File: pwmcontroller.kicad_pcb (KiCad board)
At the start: 2 copper layers, 35.1 x 44.5 mm, 19 parts, among them J1 CONN_01X04, J2 CONN_01X04, U1 WPMIx9200501S, U2 NE555

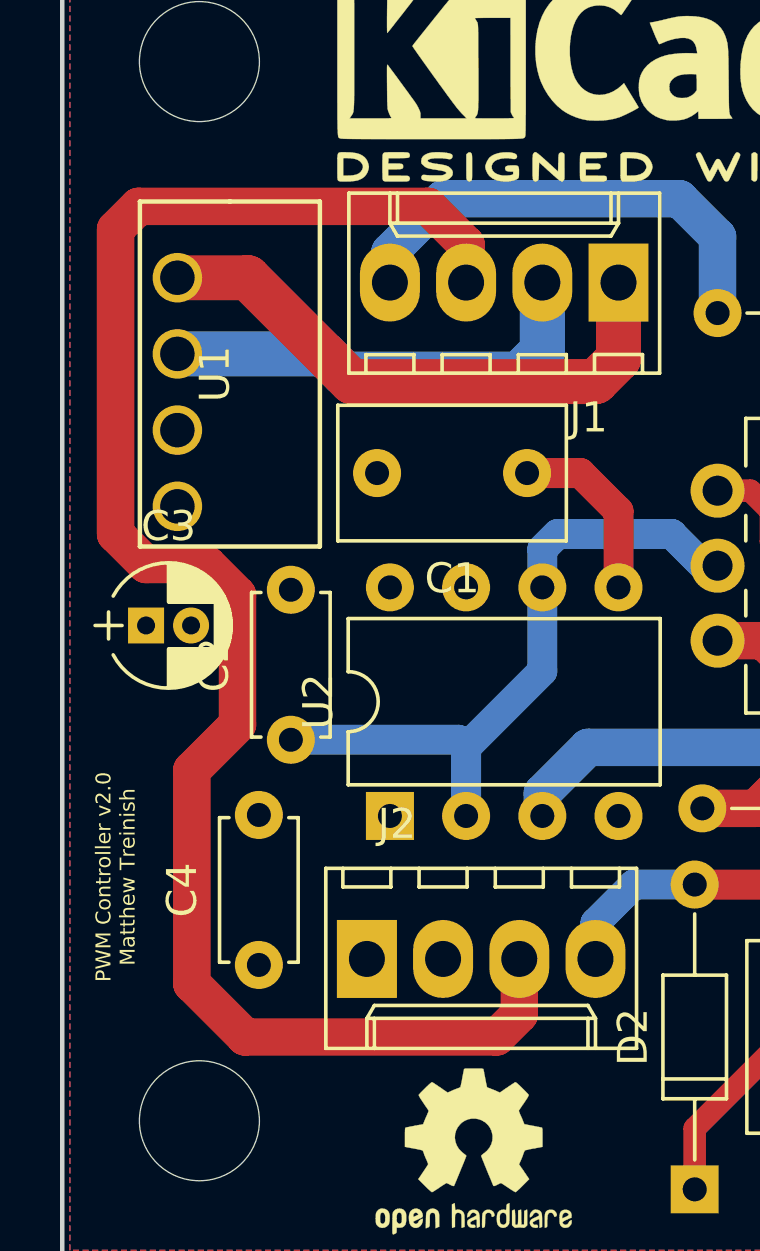
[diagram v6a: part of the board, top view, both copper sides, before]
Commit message: Fix isolated C3 ground pin on PCB
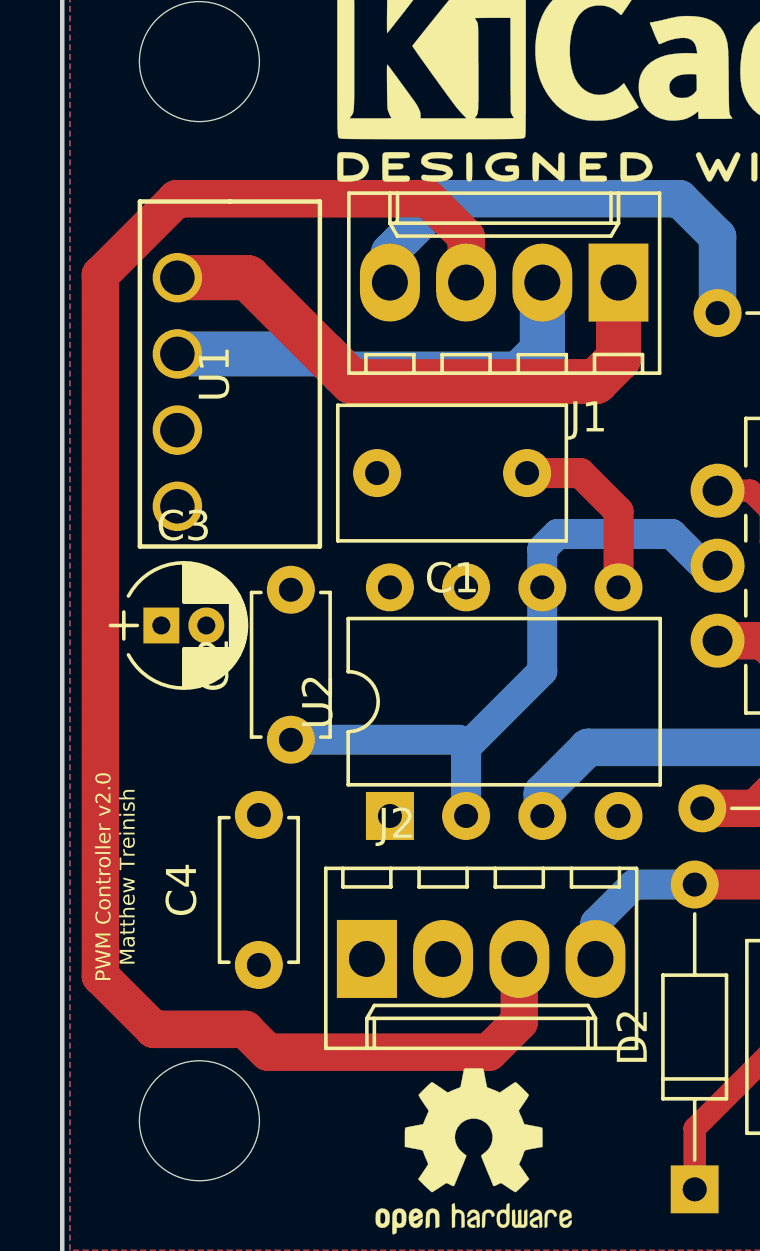
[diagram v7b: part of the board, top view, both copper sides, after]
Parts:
- moved C3 0.51 mm to (142.7, 113.3)
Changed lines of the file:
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@@
   (general
     (links 26)
-    (no_connects 1)
-    (area 136.603714 88.513 177.340286 135.869)
+    (no_connects 0)
+    (area 139.370999 88.513 174.765001 135.869)
     (thickness 1.6)
     (drawings 6)
-    (tracks 72)
+    (tracks 68)
     (zones 0)
     (modules 19)
@@
   (page A4)
   (layers
-    (0 F.Cu signal)
+    (0 F.Cu signal hide)
     (31 B.Cu signal)
-    (32 B.Adhes user)
+    (32 B.Adhes user hide)
     (33 F.Adhes user)
     (34 B.Paste user)
@@
     (38 B.Mask user)
     (39 F.Mask user)
-    (40 Dwgs.User user)
-    (41 Cmts.User user)
-    (42 Eco1.User user)
-    (43 Eco2.User user)
+    (40 Dwgs.User user hide)
+    (41 Cmts.User user hide)
+    (42 Eco1.User user hide)
+    (43 Eco2.User user hide)
     (44 Edge.Cuts user)
-    (45 Margin user)
-    (46 B.CrtYd user)
-    (47 F.CrtYd user)
-    (48 B.Fab user)
-    (49 F.Fab user)
+    (45 Margin user hide)
+    (46 B.CrtYd user hide)
+    (47 F.CrtYd user hide)
+    (48 B.Fab user hide)
+    (49 F.Fab user hide)
   )
   (setup
-    (last_trace_width 0.25)
+    (last_trace_width 1.25)
     (user_trace_width 0.25)
     (user_trace_width 0.5)
@@
   )
   (module Capacitors_THT:CP_Radial_D4.0mm_P1.50mm (layer F.Cu)
-    (at 142.24 113.284)
+    (at 142.748 113.284)
     (descr "CP, Radial series, Radial, pin pitch=1.50mm, , diameter=4mm, Electrolytic Capacitor")
     (tags "CP Radial series Radial pin pitch 1.50mm  diameter 4mm Electrolytic Capacitor")
@@
   (segment (start 148.844 104.902) (end 154.686 104.902) (width 1.5) (layer B.Cu) (net 9))
   (segment (start 148.174 104.232) (end 148.844 104.902) (width 1.5) (layer B.Cu) (net 9))
-  (segment (start 152.908 101.854) (end 152.908 100.584) (width 1.25) (layer F.Cu) (net 10))
-  (segment (start 152.908 100.584) (end 151.638 99.314) (width 1.25) (layer F.Cu) (net 10))
-  (segment (start 151.638 99.314) (end 141.986 99.314) (width 1.25) (layer F.Cu) (net 10))
-  (segment (start 141.986 99.314) (end 141.224 100.076) (width 1.25) (layer F.Cu) (net 10))
-  (segment (start 141.224 100.076) (end 141.224 110.236) (width 1.25) (layer F.Cu) (net 10))
-  (segment (start 141.224 110.236) (end 142.24 111.252) (width 1.25) (layer F.Cu) (net 10))
-  (segment (start 142.24 111.252) (end 144.272 111.252) (width 1.25) (layer F.Cu) (net 10))
-  (segment (start 144.272 111.252) (end 145.288 112.268) (width 1.25) (layer F.Cu) (net 10))
-  (segment (start 145.288 112.268) (end 145.288 116.586) (width 1.25) (layer F.Cu) (net 10))
-  (segment (start 145.288 116.586) (end 143.764 118.11) (width 1.25) (layer F.Cu) (net 10))
-  (segment (start 143.764 118.11) (end 143.764 125.222) (width 1.25) (layer F.Cu) (net 10))
-  (segment (start 143.764 125.222) (end 145.542 127) (width 1.25) (layer F.Cu) (net 10))
-  (segment (start 145.542 127) (end 153.924 127) (width 1.25) (layer F.Cu) (net 10))
-  (segment (start 153.924 127) (end 154.68 126.244) (width 1.25) (layer F.Cu) (net 10))
-  (segment (start 154.68 126.244) (end 154.68 124.4) (width 1.25) (layer F.Cu) (net 10))
+  (segment (start 154.68 124.4) (end 154.68 126.498) (width 1.25) (layer F.Cu) (net 10))
+  (segment (start 152.908 100.33) (end 152.908 101.854) (width 1.25) (layer F.Cu) (net 10))
+  (segment (start 151.638 99.06) (end 152.908 100.33) (width 1.25) (layer F.Cu) (net 10))
+  (segment (start 143.256 99.06) (end 151.638 99.06) (width 1.25) (layer F.Cu) (net 10))
+  (segment (start 140.716 101.6) (end 143.256 99.06) (width 1.25) (layer F.Cu) (net 10))
+  (segment (start 140.716 124.968) (end 140.716 101.6) (width 1.25) (layer F.Cu) (net 10))
+  (segment (start 142.494 126.746) (end 140.716 124.968) (width 1.25) (layer F.Cu) (net 10))
+  (segment (start 145.542 126.746) (end 142.494 126.746) (width 1.25) (layer F.Cu) (net 10))
+  (segment (start 146.304 127.508) (end 145.542 126.746) (width 1.25) (layer F.Cu) (net 10))
+  (segment (start 153.67 127.508) (end 146.304 127.508) (width 1.25) (layer F.Cu) (net 10))
+  (segment (start 154.68 126.498) (end 153.67 127.508) (width 1.25) (layer F.Cu) (net 10))
   (segment (start 150.368 101.854) (end 150.368 100.838) (width 1.25) (layer B.Cu) (net 11))
   (segment (start 150.368 100.838) (end 152.146 99.06) (width 1.25) (layer B.Cu) (net 11))

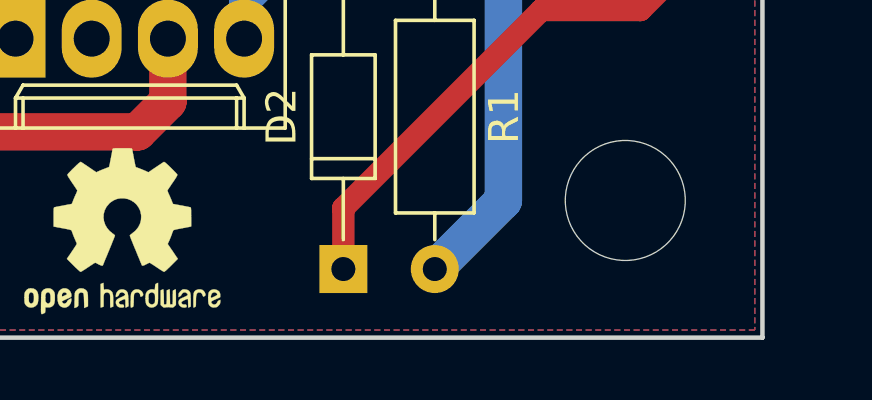
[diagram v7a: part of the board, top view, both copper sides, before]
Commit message: Add github link to PCB silkscreen
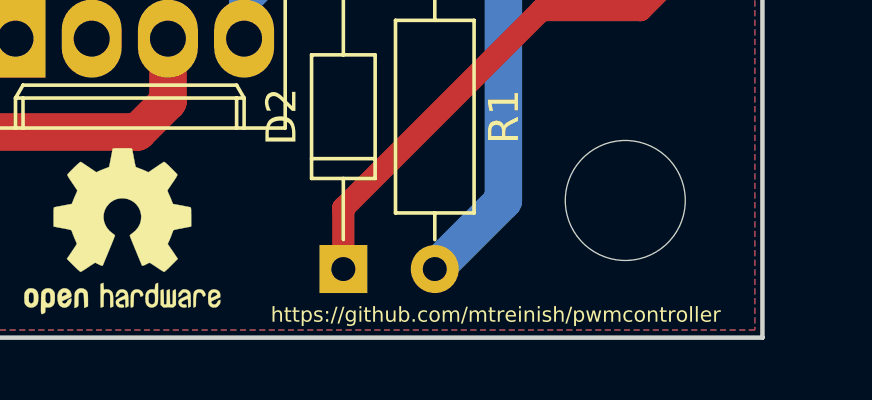
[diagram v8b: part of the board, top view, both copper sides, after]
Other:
- board text added: "https://github.com/mtreinish/pwmcontroller"
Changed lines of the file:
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@@
     (area 139.370999 88.513 174.765001 135.869)
     (thickness 1.6)
-    (drawings 6)
+    (drawings 7)
     (tracks 68)
     (zones 0)
@@
   (page A4)
   (layers
-    (0 F.Cu signal hide)
-    (31 B.Cu signal)
+    (0 F.Cu signal)
+    (31 B.Cu signal hide)
     (32 B.Adhes user hide)
     (33 F.Adhes user)
@@
   )
   (setup
-    (last_trace_width 1.25)
+    (last_trace_width 0.25)
     (user_trace_width 0.25)
     (user_trace_width 0.5)
@@
     )
   )
+  (gr_text https://github.com/mtreinish/pwmcontroller (at 165.608 133.604) (layer F.SilkS)
+    (effects (font (size 0.5 0.5) (thickness 0.125)))
+  )
   (gr_text "PWM Controller v2.0\nMatthew Treinish" (at 141.224 121.666 90) (layer F.SilkS)
